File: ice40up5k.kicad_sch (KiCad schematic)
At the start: 1 part, among them U4 ICE40UP5K-SG48ITR

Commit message: fix: adjusted positining
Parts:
- added U10, U11, U9: AD40xxBCPZ, Package_CSP:LFCSP-WD-10-1EP_3x3mm_P0.5mm_EP1.64x2.38mm, symbol Analog_ADC:AD40xxBCPZ

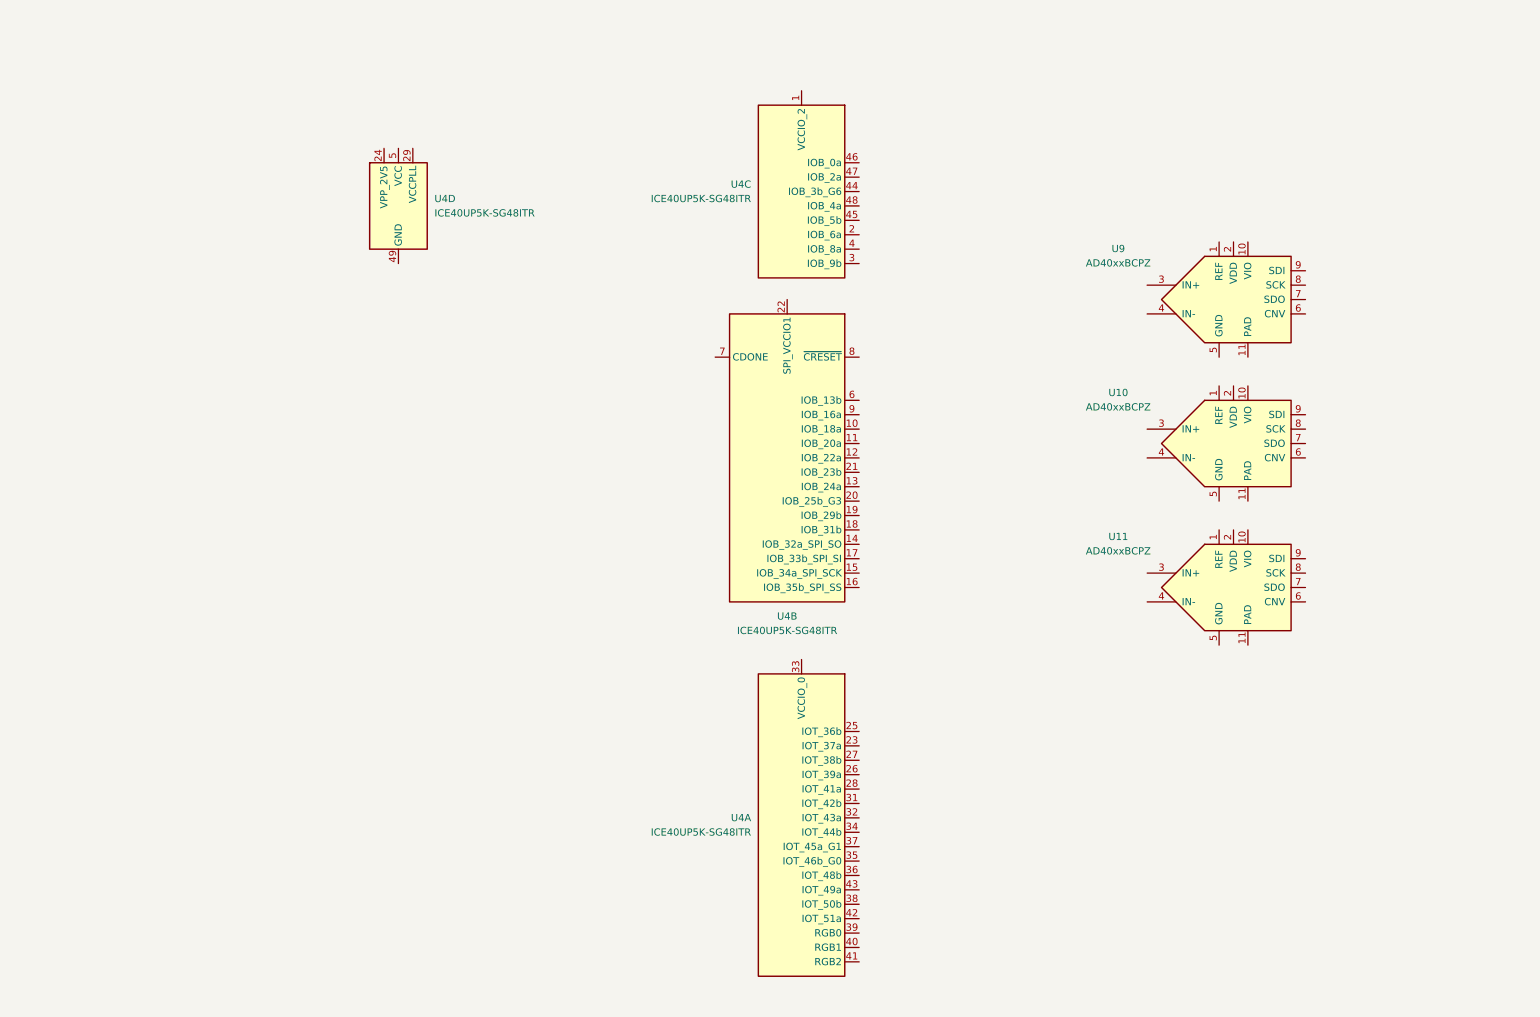
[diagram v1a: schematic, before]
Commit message: feat: done rough board placements for general shape
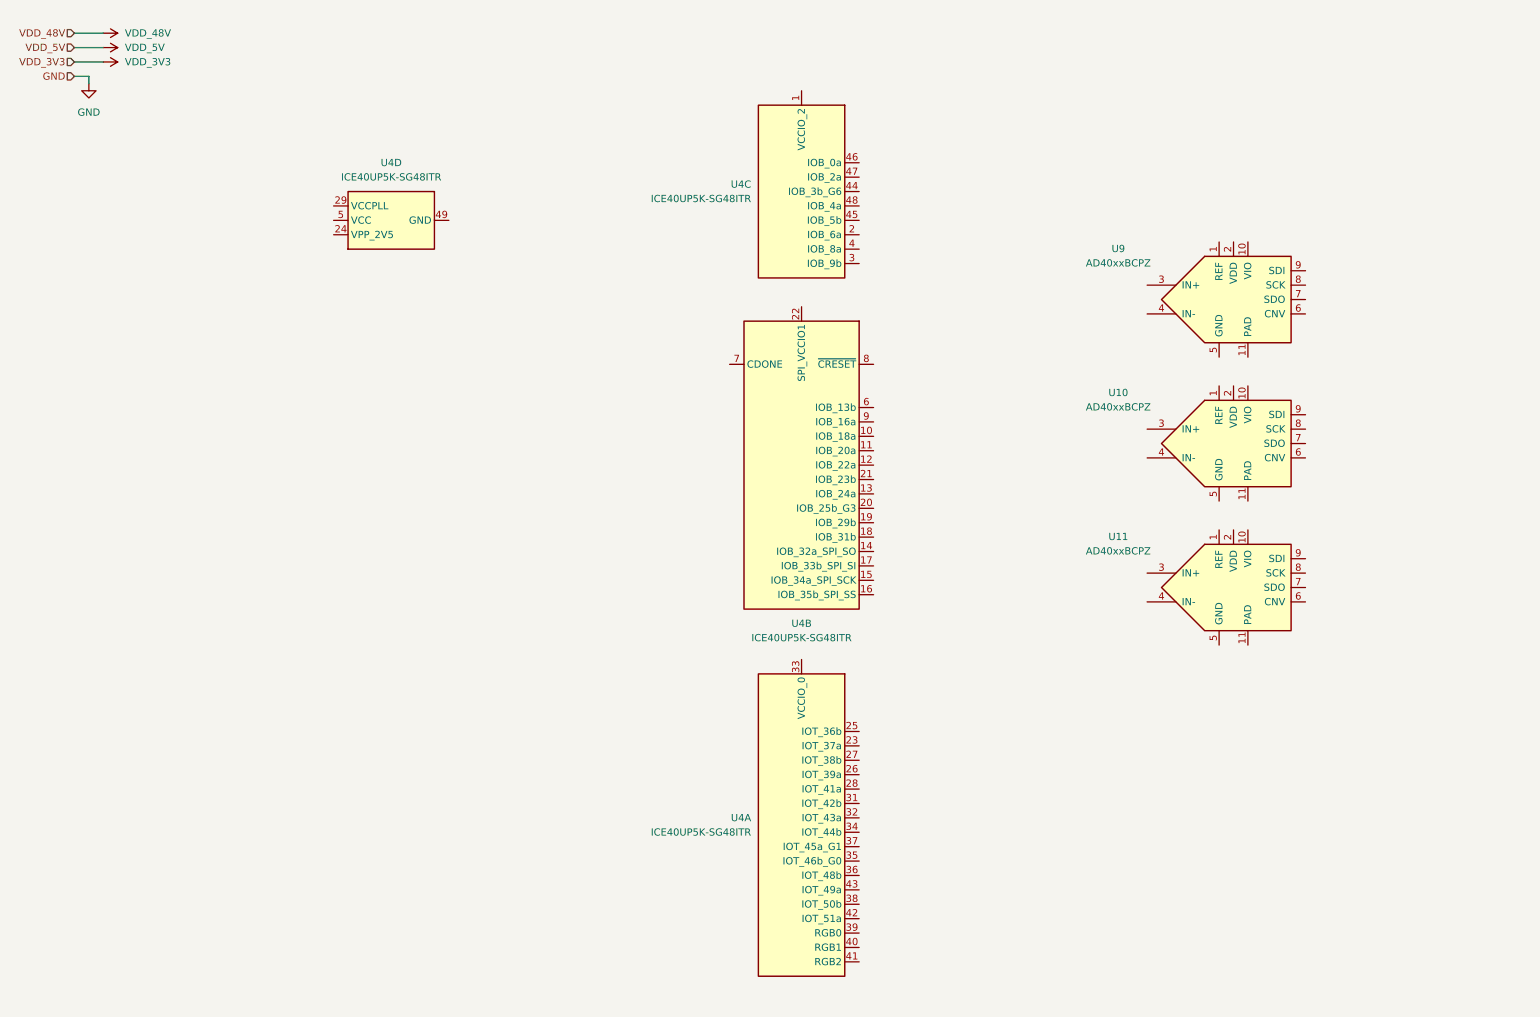
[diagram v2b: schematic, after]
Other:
- moved on the sheet: U4B, U4D

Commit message: fix: update fpga with power supply
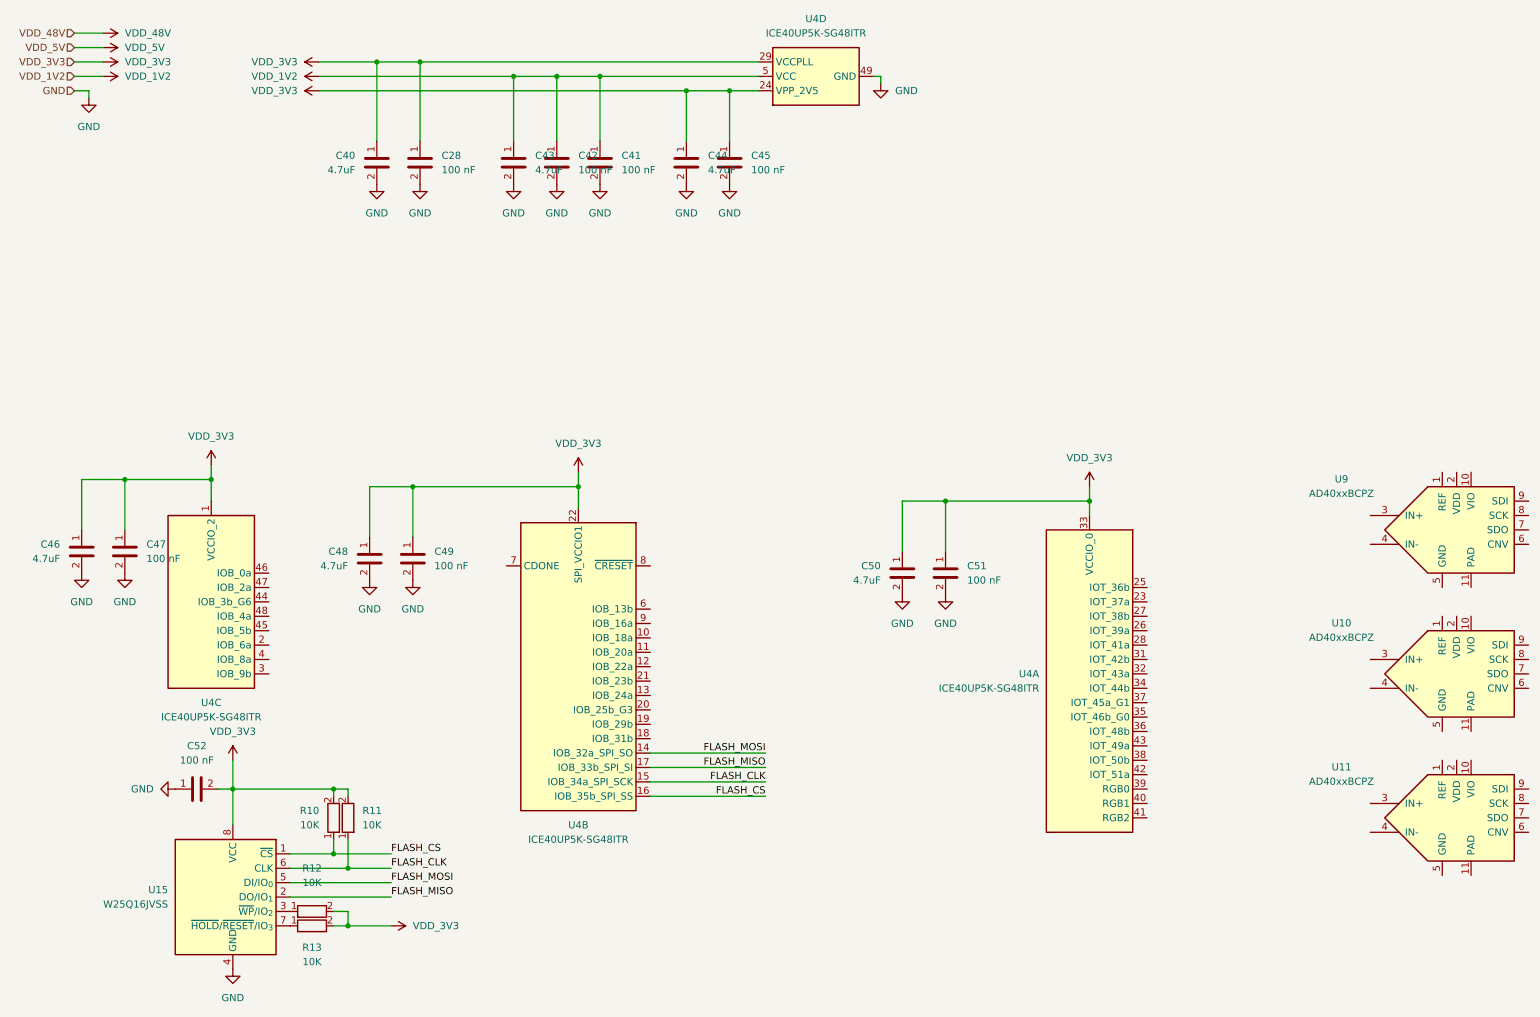
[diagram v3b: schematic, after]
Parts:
- added C28, C41, C42, C45, C47, C49, C51, C52: 100 nF, chenry-footprint-lib:C_0402, symbol 0-chenry-component-lib:C_0402_100N
- added C40, C43, C44, C46, C48, C50: 4.7uF, chenry-footprint-lib:C_0402, symbol 0-chenry-component-lib:C_0402_4U7
- added R10, R11, R12, R13: 10K, chenry-footprint-lib:R_0402, symbol 0-chenry-component-lib:R_0402_10K
- added U15: W25Q16JVSS, Package_SO:SOIC-8_5.3x5.3mm_P1.27mm, symbol Memory_Flash:W25Q16JVSS
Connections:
- net GND: now also U4.49 (GND), C28.2, C40.2, C41.2, C42.2, C43.2, C44.2, C45.2, C46.2, C47.2, C48.2, C49.2, C50.2, C51.2, C52.1, U15.4 (GND)
- net VDD_3V3: now also U4.1 (VCCIO_2), U4.22 (SPI_VCCIO1), U4.24 (VPP_2V5), U4.29 (VCCPLL), U4.33 (VCCIO_0), C28.1, C40.1, C44.1, C45.1, C46.1, C47.1, C48.1, C49.1, C50.1, C51.1, C52.2, R10.2, R11.2, R12.2, R13.2, U15.8 (VCC)
- net VDD_1V2: now reaches U4.30 (VCC), U4.5 (VCC)
- net VDD_1V2: now also C41.1, C42.1, C43.1
- net FLASH_MOSI: now reaches U4.14 (IOB_32a_SPI_SO)
- net FLASH_MOSI: now also U15.5 (DI/IO_{0})
- net FLASH_CLK: now reaches U4.15 (IOB_34a_SPI_SCK)
- net FLASH_CLK: now also R11.1, U15.6 (CLK)
- net FLASH_CS: now reaches U4.16 (IOB_35b_SPI_SS)
- net FLASH_CS: now also R10.1, U15.1 (~{CS})
- net FLASH_MISO: now reaches U4.17 (IOB_33b_SPI_SI)
- net FLASH_MISO: now also U15.2 (DO/IO_{1})
- new net: R12.1, U15.3 (~{WP}/IO_{2})
- new net: R13.1, U15.7 (~{HOLD}/~{RESET}/IO_{3})
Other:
- moved on the sheet: U10, U11, U4A, U4B, U4C, U4D, U9

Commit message: fix: fleshignout schematic for mcu, fpga and mag + peripherals
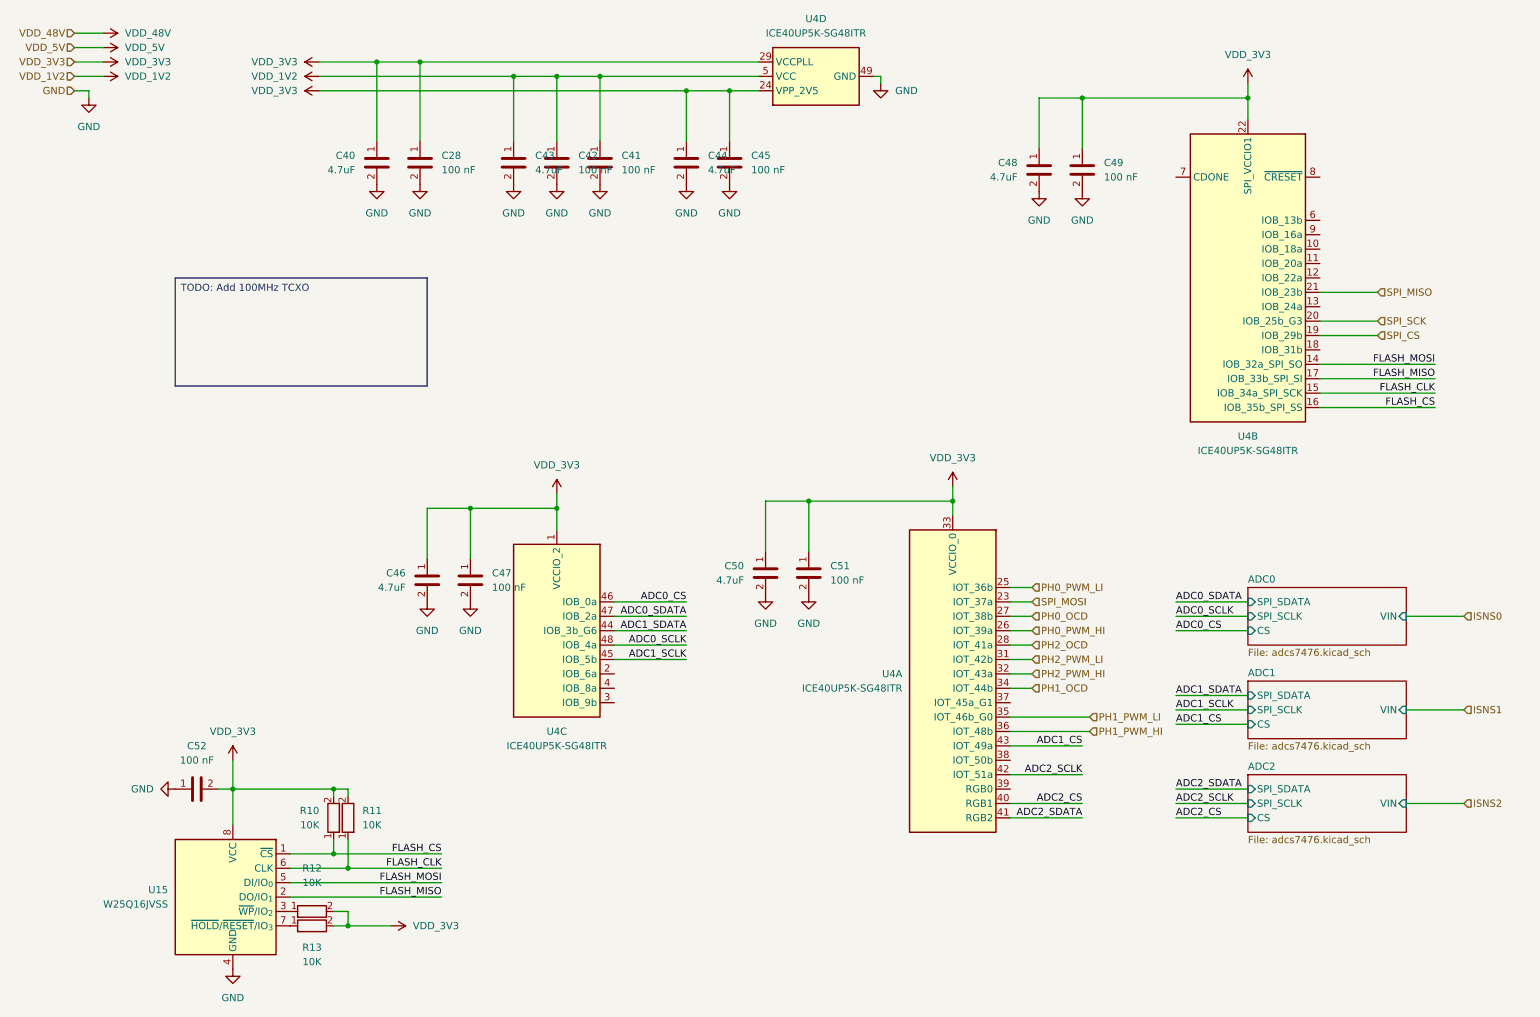
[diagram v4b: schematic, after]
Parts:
- removed U10, U11, U9: AD40xxBCPZ, Package_CSP:LFCSP-WD-10-1EP_3x3mm_P0.5mm_EP1.64x2.38mm, symbol Analog_ADC:AD40xxBCPZ
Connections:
- net SPI_MOSI: now reaches U4.23 (IOT_37a)
- net PH0_PWM_LI: now reaches U4.25 (IOT_36b)
- net PH0_PWM_HI: now reaches U4.26 (IOT_39a)
- net PH0_OCD: now reaches U4.27 (IOT_38b)
- net PH2_OCD: now reaches U4.28 (IOT_41a)
- net PH2_PWM_LI: now reaches U4.31 (IOT_42b)
- net PH2_PWM_HI: now reaches U4.32 (IOT_43a)
- net PH1_OCD: now reaches U4.34 (IOT_44b)
- net PH1_PWM_LI: now reaches U4.35 (IOT_46b_G0)
- net PH1_PWM_HI: now reaches U4.36 (IOT_48b)
- net ADC2_CS: now reaches U4.40 (RGB1)
- net ADC2_SDATA: now reaches U4.41 (RGB2)
- net ADC2_SCLK: now reaches U4.42 (IOT_51a)
- net ADC1_CS: now reaches U4.43 (IOT_49a)
- net ADC1_SDATA: now reaches U4.44 (IOB_3b_G6)
- net ADC1_SCLK: now reaches U4.45 (IOB_5b)
- net ADC0_CS: now reaches U4.46 (IOB_0a)
- net ADC0_SDATA: now reaches U4.47 (IOB_2a)
- net ADC0_SCLK: now reaches U4.48 (IOB_4a)
- net SPI_CS: now reaches U4.19 (IOB_29b)
- net SPI_SCK: now reaches U4.20 (IOB_25b_G3)
- net SPI_MISO: now reaches U4.21 (IOB_23b)
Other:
- added sheet ADC0 (adcs7476.kicad_sch)
- added sheet ADC1 (adcs7476.kicad_sch)
- added sheet ADC2 (adcs7476.kicad_sch)
- moved on the sheet: C46, C47, C48, C49, C50, C51, U4A, U4B, U4C
